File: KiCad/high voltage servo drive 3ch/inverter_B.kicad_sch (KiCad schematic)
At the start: 50 parts, among them U17 IPM

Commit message: prepare rev0.1 for manufacturing
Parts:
- C140, C141, C142, C143, C144, C145, C162: Generic Allowed? (none) -> yes; LCSC# (none) -> C106205; Manufacturer (none) -> YAGEO; Part number (none) -> CC0402KRX7R9BB102; cost (none) -> 0.001
- C146, C148, C151, C161: Generic Allowed? (none) -> yes; LCSC# C7393943 -> C50254; Manufacturer (none) -> Samsung Electro-Mechanics; Part number (none) -> CL31B225KBHNNNE; cost (none) -> 0.03
- C147, C149, C150, C152, C154, C155, C156, C160: Generic Allowed? (none) -> yes; LCSC# (none) -> C105882; Manufacturer (none) -> YAGEO; Part number (none) -> CC0402KRX5R9BB104; cost (none) -> 0.003
- C153, C163: Generic Allowed? (none) -> yes; LCSC# C473196 -> C7471876; Manufacturer (none) -> KNSCHA; Part number (none) -> 189RV0014; cost (none) -> 0.05
- C157, C158: Generic Allowed? (none) -> yes; Manufacturer (none) -> HUI JU; Part number (none) -> NV1812B104K102CEMN; cost (none) -> 0.1447
- C159, C196: Generic Allowed? (none) -> yes; LCSC# (none) -> C60133; Manufacturer (none) -> YAGEO; Part number (none) -> CC0402KRX7R9BB103; cost (none) -> 0.001
- D40, D41, D42, D43: Generic Allowed? (none) -> yes; LCSC# SMA2Z22A -> C7440711; Manufacturer (none) -> XCH; Part number (none) -> SMA2Z22A; cost (none) -> 0.07
- FB7, FB8: value FerriteBead -> 0; Generic Allowed? (none) -> yes; LCSC# C963878 -> C2907406; Manufacturer (none) -> FOJAN; Part number (none) -> FRC1206P000 TS; cost (none) -> 0.0015
- NT1, NT5, NT6: now not fitted
- R100, R101, R102, R103, R104, R105, R107: value 100 -> 120; Generic Allowed? (none) -> yes; LCSC# (none) -> C114758; Manufacturer (none) -> YAGEO; Part number (none) -> RC0402FR-07120RL; cost (none) -> 0.0008
- R106, R139: Generic Allowed? (none) -> yes; LCSC# (none) -> C105873; Manufacturer (none) -> YAGEO; Part number (none) -> RC0402JR-075K1L; cost (none) -> 0.0006
- R108, R109, R110, R111, R112, R113: Generic Allowed? (none) -> yes, 1% or better; LCSC # C7419996 -> (none); LCSC# (none) -> C7419996; Manufacturer (none) -> FOJAN; Part number (none) -> FRM121WFR005TM; cost (none) -> 0.03
- U17: Manufacturer (none) -> ONSEMI; now not fitted

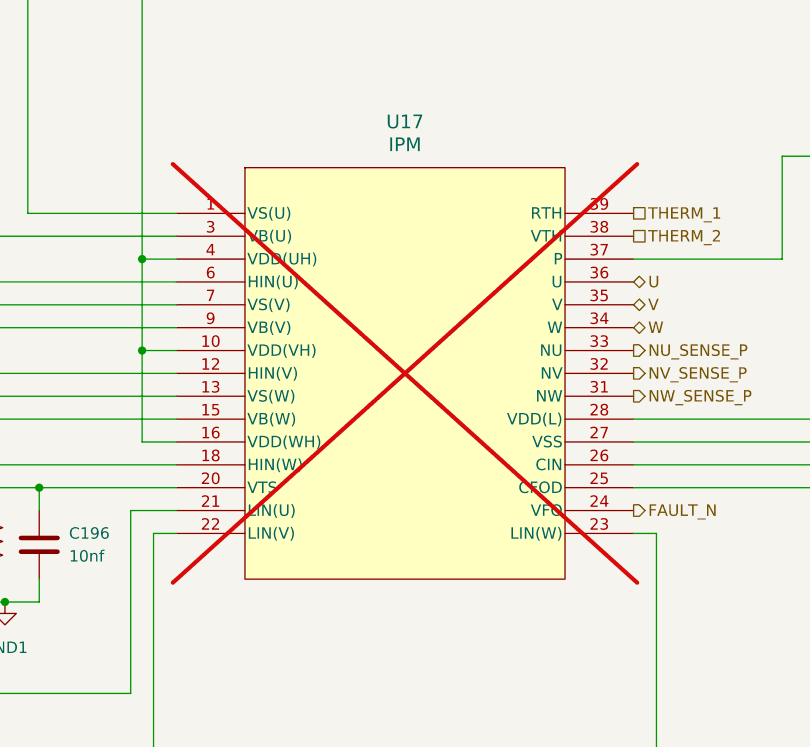
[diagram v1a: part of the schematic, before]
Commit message: update BOM and change transceivers
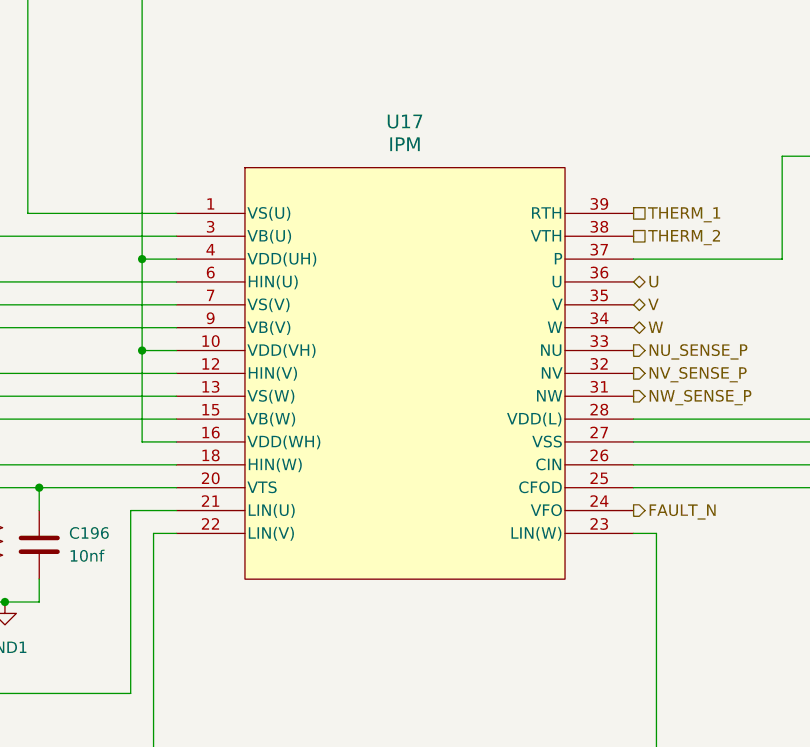
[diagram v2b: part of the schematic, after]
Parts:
- FB7, FB8: LCSC# C2907406 -> C2907288; Part number FRC1206P000 TS -> FRC0805P000 TS
- U17: footprint footprints:DIP39_54.5X31.0_MODGC_OSI -> DIP39_54.5X31.0_MODGC_OSI; now fitted
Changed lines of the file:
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@@
 		(in_bom yes)
 		(on_board yes)
-		(dnp yes)
+		(dnp no)
 		(fields_autoplaced yes)
 		(property "Reference" "U17"
@@
 			)
 		)
-		(property "Footprint" "footprints:DIP39_54.5X31.0_MODGC_OSI"
+		(property "Footprint" "DIP39_54.5X31.0_MODGC_OSI"
 			(at 184.15 121.92 0)
 			(effects
@@
 			)
 		)
-		(property "Datasheet" "IPM"
+		(property "Datasheet" "NFAM3065L4BT"
 			(at 184.15 121.92 0)
 			(effects
@@
 			)
 		)
-		(property "Description" "50v"
+		(property "Description" "Unpolarized capacitor"
 			(at 106.68 157.48 0)
 			(effects
@@
 			)
 		)
-		(property "Description" "50v"
+		(property "Description" "Unpolarized capacitor"
 			(at 116.84 203.2 0)
 			(effects
@@
 			)
 		)
-		(property "Description" "low inductance type"
+		(property "Description" "Resistor, US symbol"
 			(at 344.17 80.01 0)
 			(effects
@@
 			)
 		)
-		(property "Description" "low inductance type"
+		(property "Description" "Resistor, US symbol"
 			(at 344.17 58.42 0)
 			(effects
@@
 			)
 		)
-		(property "Description" "50v"
+		(property "Description" "Unpolarized capacitor"
 			(at 328.93 158.75 0)
 			(effects
@@
 			)
 		)
-		(property "Description" "50v"
+		(property "Description" "Unpolarized capacitor"
 			(at 184.15 85.09 0)
 			(effects
@@
 			)
 		)
-		(property "Description" "63v"
+		(property "Description" "Polarized capacitor"
 			(at 335.28 143.51 0)
 			(effects
@@
 			)
 		)
-		(property "Description" "50v"
+		(property "Description" "Unpolarized capacitor"
 			(at 106.68 203.2 0)
 			(effects
@@
 			)
 		)
-		(property "Description" "50v"
+		(property "Description" "Unpolarized capacitor"
 			(at 184.15 73.66 0)
 			(effects
@@
 			)
 		)
-		(property "Description" "50v"
+		(property "Description" "Unpolarized capacitor"
 			(at 148.59 156.21 0)
 			(effects
@@
 			)
 		)
-		(property "Description" "low inductance type"
+		(property "Description" "Resistor, US symbol"
 			(at 344.17 93.98 0)
 			(effects
@@
 			)
 		)
-		(property "Description" "50v"
+		(property "Description" "Unpolarized capacitor"
 			(at 140.97 85.09 0)
 			(effects
@@
 			)
 		)
-		(property "Description" "50v"
+		(property "Description" "Unpolarized capacitor"
 			(at 184.15 62.23 0)
 			(effects
@@
 			)
 		)
-		(property "Description" "low inductance type"
+		(property "Description" "Resistor, US symbol"
 			(at 344.17 76.2 0)
 			(effects
@@
 			)
 		)
-		(property "Description" "50v"
+		(property "Description" "Unpolarized capacitor"
 			(at 152.4 85.09 0)
 			(effects
@@
 			)
 		)
-		(property "Description" "50v"
+		(property "Description" "Unpolarized capacitor"
 			(at 323.85 143.51 0)
 			(effects
@@
 			)
 		)
-		(property "Description" "50v"
+		(property "Description" "Unpolarized capacitor"
 			(at 316.23 143.51 0)
 			(effects
@@
 			)
 		)
-		(property "LCSC#" "C2907406"
+		(property "LCSC#" "C2907288"
 			(at 316.23 134.62 0)
 			(effects
@@
 			)
 		)
-		(property "Part number" "FRC1206P000 TS"
+		(property "Part number" "FRC0805P000 TS"
 			(at 316.23 134.62 0)
 			(effects
@@
 			)
 		)
-		(property "Description" "50v"
+		(property "Description" "Unpolarized capacitor"
 			(at 163.83 85.09 0)
 			(effects
@@
 			)
 		)
-		(property "Description" "50v"
+		(property "Description" "Unpolarized capacitor"
 			(at 96.52 157.48 0)
 			(effects
@@
 			)
 		)
-		(property "Description" "50v"
+		(property "Description" "Unpolarized capacitor"
 			(at 152.4 73.66 0)
 			(effects
@@
 			)
 		)
-		(property "Description" "low inductance type"
+		(property "Description" "Resistor, US symbol"
 			(at 344.17 97.79 0)
 			(effects
@@
 			)
 		)
-		(property "Description" "50v"
+		(property "Description" "Unpolarized capacitor"
 			(at 168.91 158.75 0)
 			(effects
@@
 			)
 		)
-		(property "Description" "50v"
+		(property "Description" "Unpolarized capacitor"
 			(at 163.83 73.66 0)
 			(effects
@@
 			)
 		)
-		(property "LCSC#" "C2907406"
+		(property "LCSC#" "C2907288"
 			(at 176.53 34.29 0)
 			(effects
@@
 			)
 		)
-		(property "Part number" "FRC1206P000 TS"
+		(property "Part number" "FRC0805P000 TS"
 			(at 176.53 34.29 0)
 			(effects
@@
 			)
 		)
-		(property "Description" "50v"
+		(property "Description" "Unpolarized capacitor"
 			(at 96.52 203.2 0)
 			(effects
@@
 			)
 		)
-		(property "Description" "1kv"
+		(property "Description" "Unpolarized capacitor"
 			(at 273.05 120.65 0)
 			(effects
@@
 			)
 		)
-		(property "Description" "50v"
+		(property "Description" "Unpolarized capacitor"
 			(at 307.34 168.91 0)
 			(effects
@@
 			)
 		)
-		(property "Description" "50v"
+		(property "Description" "Unpolarized capacitor"
 			(at 140.97 73.66 0)
 			(effects
@@
 			)
 		)
-		(property "Description" "1kv"
+		(property "Description" "Unpolarized capacitor"
 			(at 285.75 120.65 0)
 			(effects
@@
 			)
 		)
-		(property "Description" "low inductance type"
+		(property "Description" "Resistor, US symbol"
 			(at 344.17 62.23 0)
 			(effects
@@
 			)
 		)
-		(property "Description" "50v"
+		(property "Description" "Unpolarized capacitor"
 			(at 116.84 157.48 0)
 			(effects
@@
 			)
 		)
-		(property "Description" "63v"
+		(property "Description" "Polarized capacitor"
 			(at 184.15 49.53 0)
 			(effects
